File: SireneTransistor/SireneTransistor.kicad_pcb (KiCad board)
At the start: 2 copper layers, 72.4 x 30.7 mm, 18 parts, among them Q1 2N3906, Q2 2N3904, Q3 2N3906, SW1 

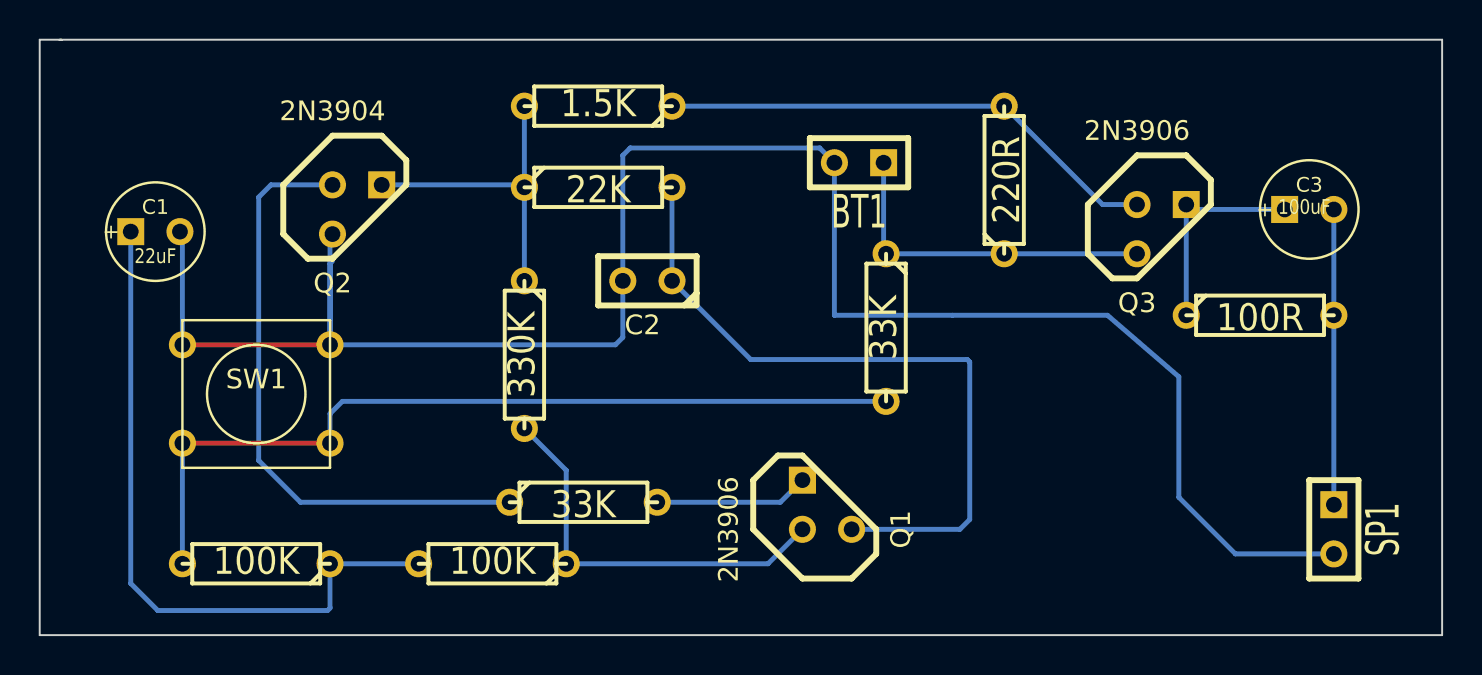
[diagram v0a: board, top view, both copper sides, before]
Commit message: Acerto da espessura das trilhas
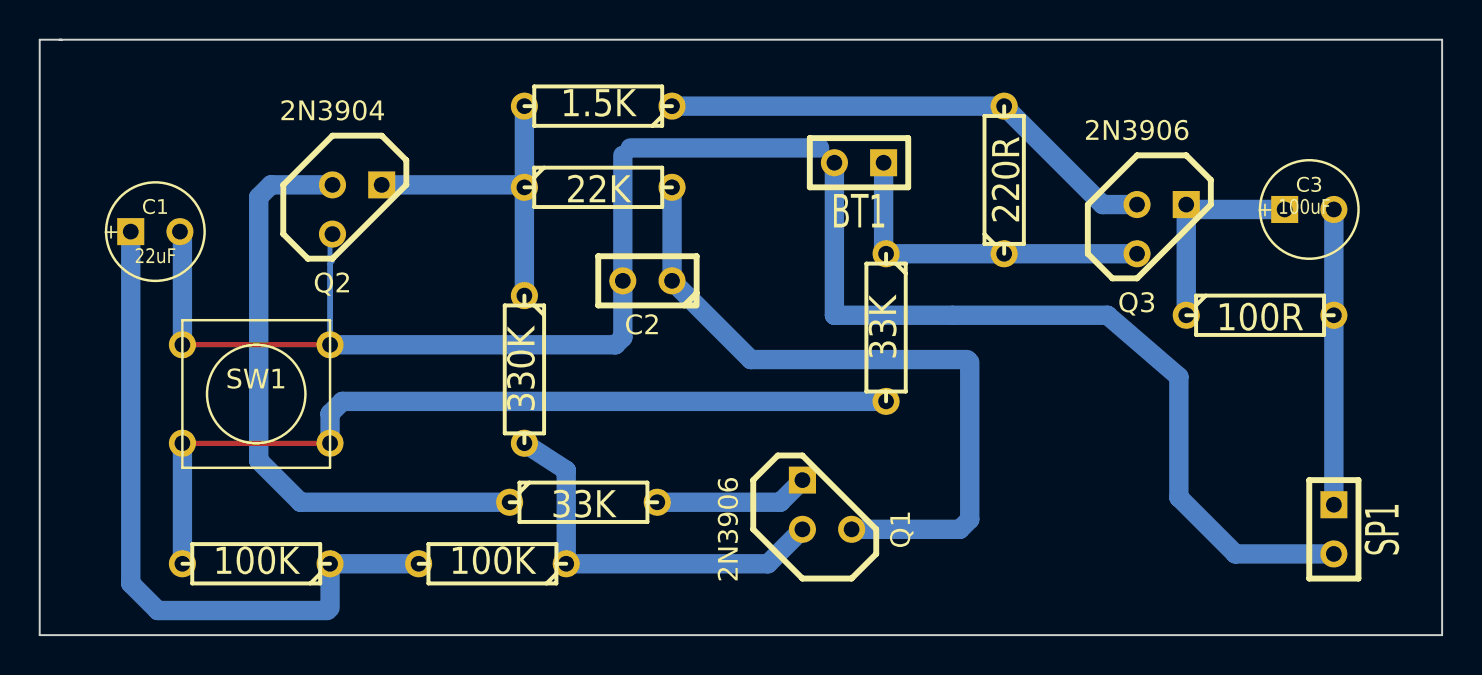
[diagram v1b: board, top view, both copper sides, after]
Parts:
- moved R4 0.76 mm to (104.0, 52.5)
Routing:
- net N-000002: track 16.2 -> 16.9 mm
